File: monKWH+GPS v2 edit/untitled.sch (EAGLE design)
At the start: 67 parts, among them J1 U.FL-R-SMT(01), J2 DCJ0202, J3 2172034-1, J5 RJ45-8N-B, Q1 MMBT3904, Q2 MMBT3904, Q3 12MHz, U1 RT9193-33GB, U2 RT9193-33GB, U3 RT9193-33GB, U4 L80-R, U5 MAX232CSE, X1 MSTBA2

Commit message: Add files via upload
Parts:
- removed C28: 10uF/16V, rcl:CPOL-EU153CLV-0505
- removed C29: 0.1uf/16V, rcl:CPOL-EU153CLV-0505
- added C4: (no value), rcl:CPOL-EUE2.5-7
- added U6: RA-01H, RA-01H:RA-01H
- added X2: (no value), EYR_Conectores:5555164-1
- C13, C15, C16: value (none) -> 100nf
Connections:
- new net N$11: C4.+, PS1.+V(CAP)
- new net N$7: C4.-, PS1.-V(CAP)
- net 3V3-LAN-GPS: no longer C28.+, C29.+
- net 3V3-LORA-RS232: now also U6.3.3V
- net ANT: now also U6.ANT
- net GND: now also U6.GND; no longer C28.-, C29.-
- net LORA_DI0: now also U6.DIO0
- net LORA_DI1: now also U6.DIO1
- net MISO_VSPI: now also LORA-NICERF-V1.MISO, MD1.IO19, U6.MISO; no longer LORA-NICERF-V1.MOSI, MD1.IO23
- net MOSI_VSPI: now also LORA-NICERF-V1.MOSI, MD1.IO23, U6.MOSI; no longer LORA-NICERF-V1.MISO, MD1.IO19
- net RST_LORA: now also U6.RESET
- net SCK_VSPI: now also U6.SCK
- net SS_LORA: now also U6.NSS
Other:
- moved on the sheet: D1, D6, GND-MK7, GND_MK10, POWER, PROSES, R12, R13, R3, R4, R5, RX_MK10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

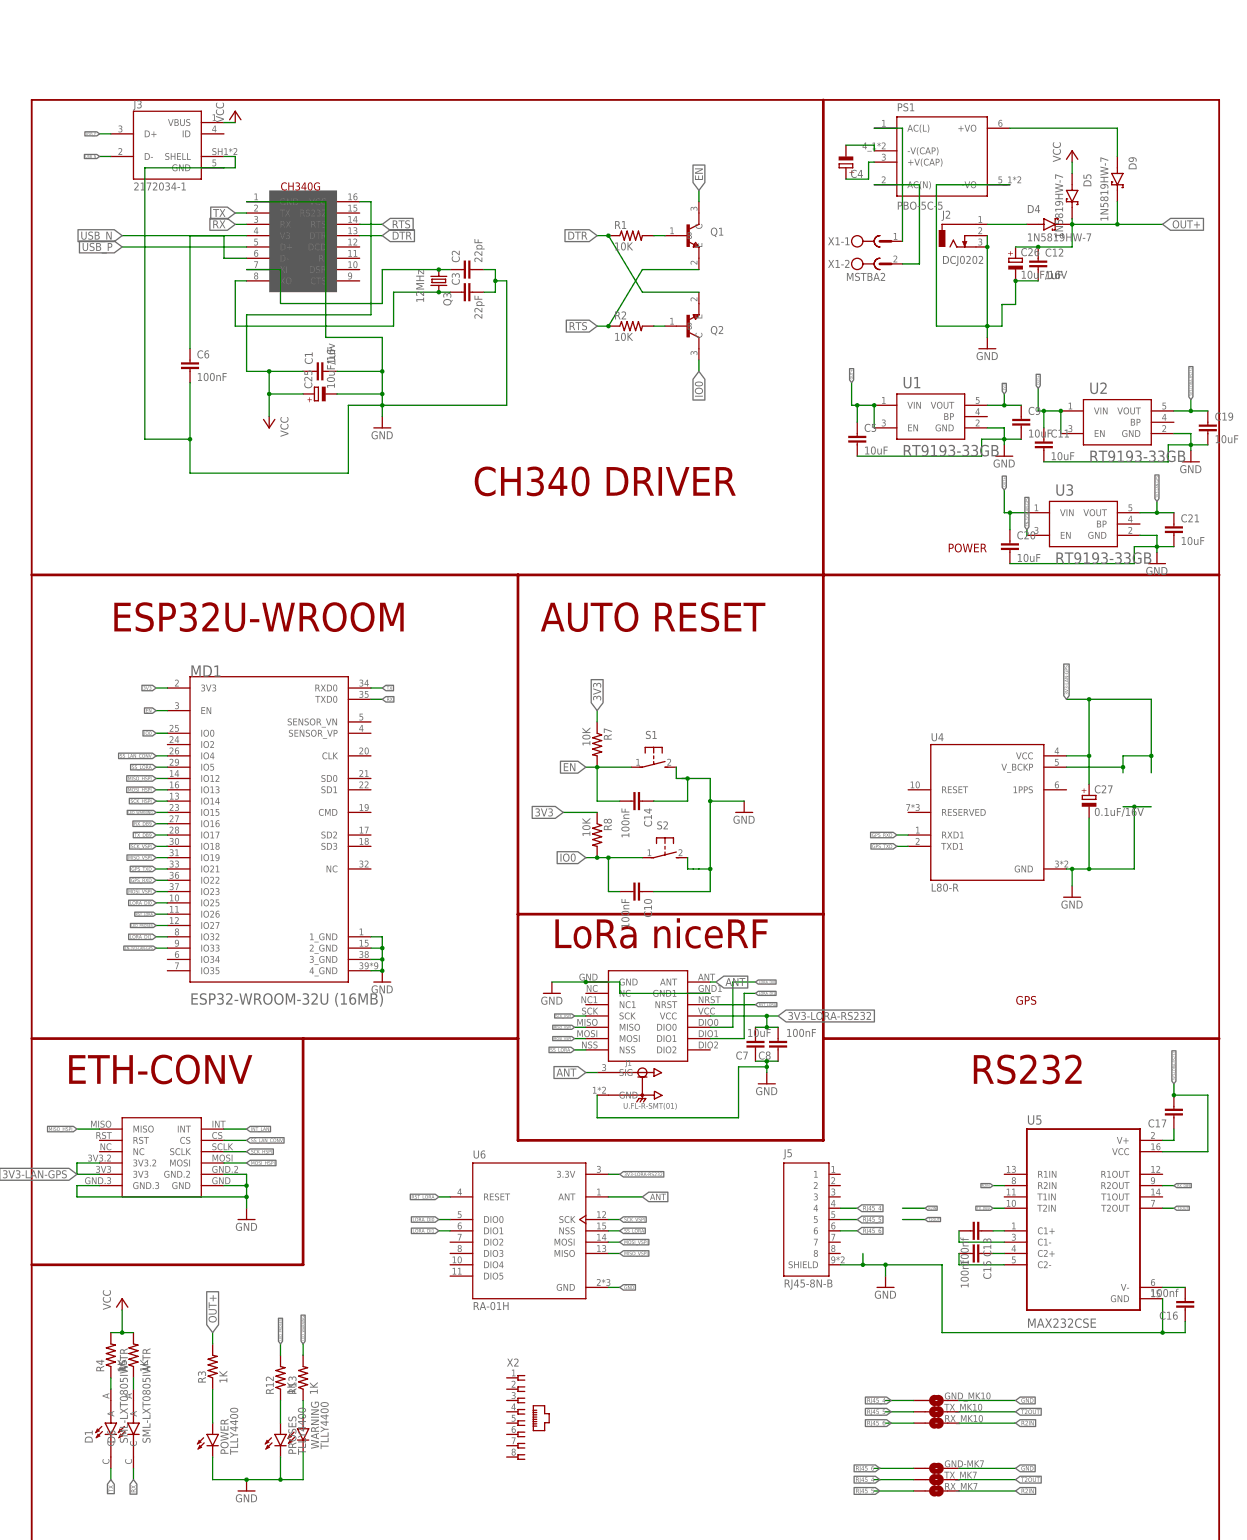
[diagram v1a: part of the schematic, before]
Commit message: change mini usb to micro usb
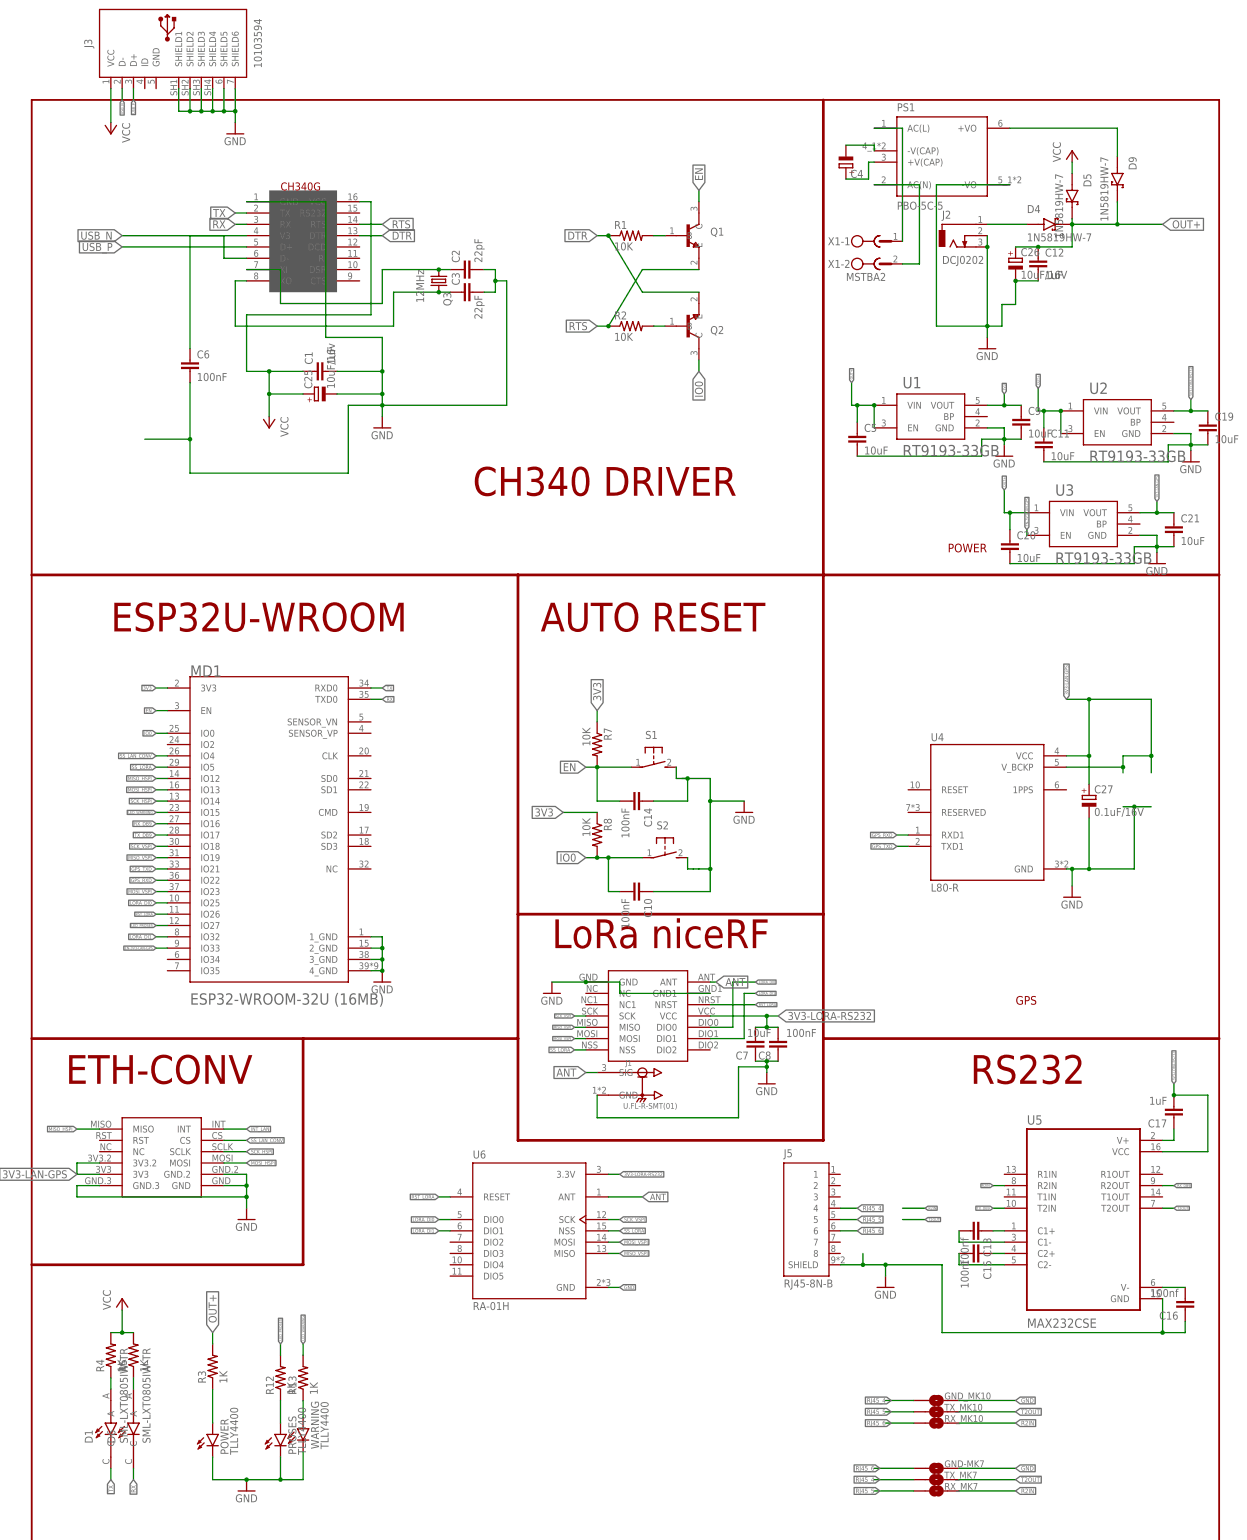
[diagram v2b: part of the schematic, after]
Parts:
- removed X2: (no value), EYR_Conectores:5555164-1
- C17: value (none) -> 1uF
- J3: value 2172034-1 -> 10103594; device 2172034-1:2172034-1 -> Connector_USB:10103594
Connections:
- net GND: now also J3.SHIELD1, J3.SHIELD2, J3.SHIELD3, J3.SHIELD4, J3.SHIELD5, J3.SHIELD6; no longer J3.GND, J3.SHELL
- net VCC: now also J3.VCC; no longer J3.VBUS
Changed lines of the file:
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@@
 <?xml version="1.0" encoding="utf-8"?>
 <!DOCTYPE eagle SYSTEM "eagle.dtd">
-<eagle version="9.5.2">
+<eagle version="9.6.2">
 <drawing>
 <settings>
@@
 <part name="R12" library="adafruit" library_urn="urn:adsk.eagle:library:420" deviceset="R-US_" device="M0805" package3d_urn="urn:adsk.eagle:package:6240587/1" value="1K"/>
 <part name="R13" library="adafruit" library_urn="urn:adsk.eagle:library:420" deviceset="R-US_" device="M0805" package3d_urn="urn:adsk.eagle:package:6240587/1" value="1K"/>
-<part name="J3" library="2172034-1" deviceset="2172034-1" device=""/>
 <part name="P+5" library="supply1" library_urn="urn:adsk.eagle:library:371" deviceset="VCC" device=""/>
 <part name="D5" library="1N5819HW-7" deviceset="1N5819HW-7" device=""/>
@@
 <part name="C15" library="rcl" library_urn="urn:adsk.eagle:library:334" deviceset="C-EU" device="C0805" package3d_urn="urn:adsk.eagle:package:23617/2" value="100nf"/>
 <part name="C16" library="rcl" library_urn="urn:adsk.eagle:library:334" deviceset="C-EU" device="C0805" package3d_urn="urn:adsk.eagle:package:23617/2" value="100nf"/>
-<part name="C17" library="rcl" library_urn="urn:adsk.eagle:library:334" deviceset="C-EU" device="C0805" package3d_urn="urn:adsk.eagle:package:23617/2"/>
+<part name="C17" library="rcl" library_urn="urn:adsk.eagle:library:334" deviceset="C-EU" device="C0805" package3d_urn="urn:adsk.eagle:package:23617/2" value="1uF"/>
 <part name="RX_MK7" library="Ai_Connectors" deviceset="1X02-SJ-NO" device=""/>
 <part name="TX_MK7" library="Ai_Connectors" deviceset="1X02-SJ-NO" device=""/>
@@
 <part name="C4" library="rcl" library_urn="urn:adsk.eagle:library:334" deviceset="CPOL-EU" device="E2.5-7" package3d_urn="urn:adsk.eagle:package:23345/1"/>
 <part name="U6" library="RA-01H" deviceset="RA-01H" device=""/>
-<part name="X2" library="EYR_Conectores" deviceset="5555164" device="-1"/>
+<part name="J3" library="Connector_USB" library_urn="urn:adsk.eagle:library:27510300" deviceset="10103594" device="" package3d_urn="urn:adsk.eagle:package:27659499/2"/>
+<part name="GND13" library="supply1" library_urn="urn:adsk.eagle:library:371" deviceset="GND" device=""/>
 </parts>
 <sheets>
@@
 <attribute name="VALUE" x="-65.278" y="-100.33" size="1.778" layer="96" rot="R90"/>
 </instance>
-<instance part="J3" gate="G$1" x="-99.06" y="180.34" smashed="yes">
-<attribute name="NAME" x="-106.688590625" y="188.6043" size="1.78" layer="95"/>
-<attribute name="VALUE" x="-106.68643125" y="170.1714" size="1.7795" layer="96"/>
-</instance>
-<instance part="P+5" gate="VCC" x="-83.82" y="187.96" smashed="yes">
-<attribute name="VALUE" x="-86.36" y="185.42" size="1.778" layer="96" rot="R90"/>
+<instance part="P+5" gate="VCC" x="-111.76" y="182.88" smashed="yes" rot="R180">
+<attribute name="VALUE" x="-109.22" y="185.42" size="1.778" layer="96" rot="R270"/>
 </instance>
 <instance part="D5" gate="G$1" x="104.14" y="168.91" smashed="yes" rot="R270">
@@
 <attribute name="VALUE" x="-30.48" y="-81.28" size="1.778" layer="96"/>
 </instance>
-<instance part="X2" gate="G$1" x="-20.32" y="-104.14" smashed="yes">
-<attribute name="NAME" x="-22.86" y="-93.98" size="1.778" layer="95"/>
-<attribute name="VALUE" x="-22.86" y="-117.348" size="1.778" layer="96"/>
+<instance part="J3" gate="G$1" x="-99.06" y="203.2" smashed="yes" rot="R90">
+<attribute name="NAME" x="-116.84" y="203.2" size="1.778" layer="95" rot="R90" align="center"/>
+<attribute name="VALUE" x="-78.74" y="203.2" size="1.778" layer="96" rot="R90" align="center"/>
+</instance>
+<instance part="GND13" gate="1" x="-83.82" y="182.88" smashed="yes">
+<attribute name="VALUE" x="-86.36" y="180.34" size="1.778" layer="96"/>
 </instance>
 </instances>
@@
 <wire x1="-60.96" y1="124.46" x2="-50.8" y2="124.46" width="0.1524" layer="91"/>
 <junction x="-50.8" y="124.46"/>
-<pinref part="J3" gate="G$1" pin="SHELL"/>
-<wire x1="-86.36" y1="177.8" x2="-83.82" y2="177.8" width="0.1524" layer="91"/>
-<pinref part="J3" gate="G$1" pin="GND"/>
-<wire x1="-86.36" y1="175.26" x2="-83.82" y2="175.26" width="0.1524" layer="91"/>
-<wire x1="-83.82" y1="177.8" x2="-83.82" y2="175.26" width="0.1524" layer="91"/>
-<wire x1="-86.36" y1="175.26" x2="-104.14" y2="175.26" width="0.1524" layer="91"/>
-<wire x1="-104.14" y1="175.26" x2="-104.14" y2="114.3" width="0.1524" layer="91"/>
 <wire x1="-104.14" y1="114.3" x2="-93.98" y2="114.3" width="0.1524" layer="91"/>
 <junction x="-93.98" y="114.3"/>
@@
 <label x="2.54" y="-76.2" size="0.8128" layer="95" xref="yes"/>
 </segment>
+<segment>
+<pinref part="J3" gate="G$1" pin="SHIELD1"/>
+<wire x1="-96.52" y1="193.04" x2="-96.52" y2="187.96" width="0.1524" layer="91"/>
+<wire x1="-96.52" y1="187.96" x2="-93.98" y2="187.96" width="0.1524" layer="91"/>
+<pinref part="GND13" gate="1" pin="GND"/>
+<wire x1="-93.98" y1="187.96" x2="-91.44" y2="187.96" width="0.1524" layer="91"/>
+<wire x1="-91.44" y1="187.96" x2="-88.9" y2="187.96" width="0.1524" layer="91"/>
+<wire x1="-88.9" y1="187.96" x2="-86.36" y2="187.96" width="0.1524" layer="91"/>
+<wire x1="-86.36" y1="187.96" x2="-83.82" y2="187.96" width="0.1524" layer="91"/>
+<wire x1="-83.82" y1="187.96" x2="-83.82" y2="185.42" width="0.1524" layer="91"/>
+<pinref part="J3" gate="G$1" pin="SHIELD6"/>
+<wire x1="-83.82" y1="193.04" x2="-83.82" y2="187.96" width="0.1524" layer="91"/>
+<junction x="-83.82" y="187.96"/>
+<pinref part="J3" gate="G$1" pin="SHIELD5"/>
+<wire x1="-86.36" y1="193.04" x2="-86.36" y2="187.96" width="0.1524" layer="91"/>
+<junction x="-86.36" y="187.96"/>
+<pinref part="J3" gate="G$1" pin="SHIELD4"/>
+<wire x1="-88.9" y1="193.04" x2="-88.9" y2="187.96" width="0.1524" layer="91"/>
+<junction x="-88.9" y="187.96"/>
+<pinref part="J3" gate="G$1" pin="SHIELD3"/>
+<wire x1="-91.44" y1="193.04" x2="-91.44" y2="187.96" width="0.1524" layer="91"/>
+<junction x="-91.44" y="187.96"/>
+<pinref part="J3" gate="G$1" pin="SHIELD2"/>
+<wire x1="-93.98" y1="193.04" x2="-93.98" y2="187.96" width="0.1524" layer="91"/>
+<junction x="-93.98" y="187.96"/>
+</segment>
 </net>
 <net name="USB_P" class="0">
@@
 </segment>
 <segment>
+<wire x1="-106.68" y1="193.04" x2="-106.68" y2="190.5" width="0.1524" layer="91"/>
+<label x="-106.68" y="190.5" size="0.6096" layer="95" rot="R270" xref="yes"/>
 <pinref part="J3" gate="G$1" pin="D+"/>
-<wire x1="-111.76" y1="182.88" x2="-114.3" y2="182.88" width="0.1524" layer="91"/>
-<label x="-114.3" y="182.88" size="0.6096" layer="95" rot="R180" xref="yes"/>
 </segment>
 </net>
@@
 </segment>
 <segment>
+<wire x1="-109.22" y1="193.04" x2="-109.22" y2="190.5" width="0.1524" layer="91"/>
+<label x="-109.22" y="190.5" size="0.6096" layer="95" rot="R270" xref="yes"/>
 <pinref part="J3" gate="G$1" pin="D-"/>
-<wire x1="-111.76" y1="177.8" x2="-114.3" y2="177.8" width="0.1524" layer="91"/>
-<label x="-114.3" y="177.8" size="0.6096" layer="95" rot="R180" xref="yes"/>
 </segment>
 </net>
@@
 </segment>
 <segment>
-<pinref part="J3" gate="G$1" pin="VBUS"/>
-<wire x1="-86.36" y1="185.42" x2="-83.82" y2="185.42" width="0.1524" layer="91"/>
+<wire x1="-111.76" y1="193.04" x2="-111.76" y2="185.42" width="0.1524" layer="91"/>
 <pinref part="P+5" gate="VCC" pin="VCC"/>
-</segment>
-<segment>
+<pinref part="J3" gate="G$1" pin="VCC"/>
+</segment>
+<segment>
